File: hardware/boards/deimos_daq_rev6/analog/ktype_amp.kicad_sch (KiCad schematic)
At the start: 12 parts, among them IC9001 INA826AIDR, J9001 AM-K-PCB

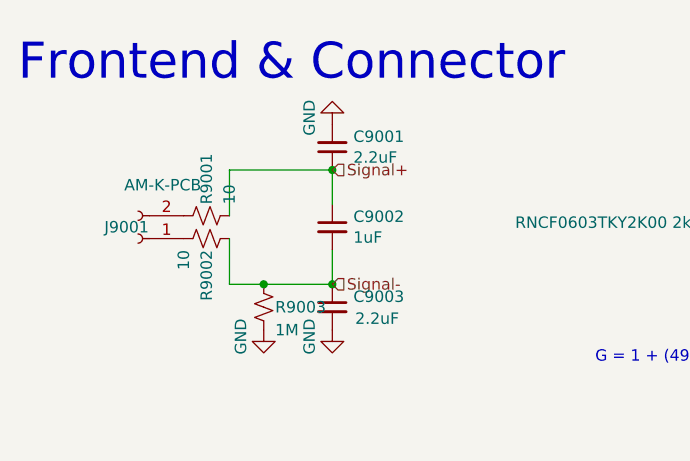
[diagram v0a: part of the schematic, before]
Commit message: move clamp diodes in schematic for filters. Add pulldown on ktype amp.
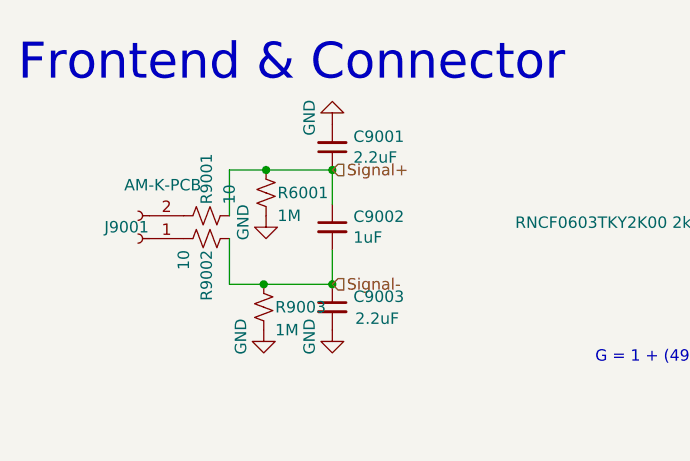
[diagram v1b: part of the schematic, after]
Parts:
- added R6001: 1M, Resistor_SMD:R_0402_1005Metric, symbol Device:R_Small_US
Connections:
- net GND: now also R6001.2
- net Signal+: now also R6001.1
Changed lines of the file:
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@@
+	)
+	(junction
+		(at 117.094 91.44)
+		(diameter 0)
+		(color 0 0 0 0)
 	)
 	(junction
@@
 	(wire
 		(pts
-			(xy 113.03 104.14) (xy 116.84 104.14)
+			(xy 117.094 91.44) (xy 124.46 91.44)
 		)
 		(stroke
@@
 	(wire
 		(pts
-			(xy 219.71 100.33) (xy 252.73 100.33)
+			(xy 113.03 104.14) (xy 116.84 104.14)
 		)
 		(stroke
@@
 	(wire
 		(pts
-			(xy 124.46 95.25) (xy 124.46 91.44)
+			(xy 219.71 100.33) (xy 252.73 100.33)
 		)
 		(stroke
@@
 	(wire
 		(pts
-			(xy 113.03 91.44) (xy 124.46 91.44)
+			(xy 124.46 95.25) (xy 124.46 91.44)
+		)
+		(stroke
+			(width 0)
+			(type default)
+		)
+	)
+	(wire
+		(pts
+			(xy 113.03 91.44) (xy 117.094 91.44)
 		)
 		(stroke
@@
 	)
 	(symbol
+		(lib_id "Device:R_Small_US")
+		(at 117.094 93.98 0)
+		(unit 1)
+		(exclude_from_sim no)
+		(in_bom yes)
+		(on_board yes)
+		(dnp no)
+		(property "Reference" "R6001"
+			(at 118.364 93.98 0)
+			(effects
+				(font
+					(size 1.27 1.27)
+				)
+				(justify left)
+			)
+		)
+		(property "Value" "1M"
+			(at 118.364 96.52 0)
+			(effects
+				(font
+					(size 1.27 1.27)
+				)
+				(justify left)
+			)
+		)
+		(property "Footprint" "Resistor_SMD:R_0402_1005Metric"
+			(at 117.094 93.98 0)
+			(effects
+				(font
+					(size 1.27 1.27)
+				)
+				(hide yes)
+			)
+		)
+		(property "Datasheet" "~"
+			(at 117.094 93.98 0)
+			(effects
+				(font
+					(size 1.27 1.27)
+				)
+				(hide yes)
+			)
+		)
+		(property "Description" ""
+			(at 117.094 93.98 0)
+			(effects
+				(font
+					(size 1.27 1.27)
+				)
+				(hide yes)
+			)
+		)
+		(pin "1"
+		)
+		(pin "2"
+		)
+		(instances
+			(project "analog_frontend_panel"
+				(path "/c241d083-1323-4b4a-a540-956d0afb7b72/15b6c474-02be-417e-bc87-8489b7b45186"
+					(reference "R6001")
+					(unit 1)
+				)
+				(path "/c241d083-1323-4b4a-a540-956d0afb7b72/3688ccee-a1b0-41d3-bce5-95bc73998b83"
+					(reference "R7001")
+					(unit 1)
+				)
+			)
+		)
+	)
+	(symbol
 		(lib_id "Device:C_Small")
 		(at 219.71 107.95 180)
@@
 					(unit 1)
 				)
+			)
+		)
+	)
+	(symbol
+		(lib_id "power:GND")
+		(at 117.094 96.52 0)
+		(unit 1)
+		(exclude_from_sim no)
+		(in_bom yes)
+		(on_board yes)
+		(dnp no)
+		(property "Reference" "#PWR6004"
+			(at 117.094 102.87 0)
+			(effects
+				(font
+					(size 1.27 1.27)
+				)
+				(hide yes)
+			)
+		)
+		(property "Value" "GND"
+			(at 114.554 95.25 90)
+			(effects
+				(font
+					(size 1.27 1.27)
+				)
+				(justify right)
+			)
+		)
+		(property "Footprint" ""
+			(at 117.094 96.52 0)
+			(effects
+				(font
+					(size 1.27 1.27)
+				)
+				(hide yes)
+			)
+		)
+		(property "Datasheet" ""
+			(at 117.094 96.52 0)
+			(effects
+				(font
+					(size 1.27 1.27)
+				)
+				(hide yes)
+			)
+		)
+		(property "Description" ""
+			(at 117.094 96.52 0)
+			(effects
+				(font
+					(size 1.27 1.27)
+				)
+				(hide yes)
+			)
+		)
+		(pin "1"
+		)
+		(instances
+			(project "analog_frontend_panel"
+				(path "/c241d083-1323-4b4a-a540-956d0afb7b72/15b6c474-02be-417e-bc87-8489b7b45186"
+					(reference "#PWR6004")
+					(unit 1)
+				)
+				(path "/c241d083-1323-4b4a-a540-956d0afb7b72/3688ccee-a1b0-41d3-bce5-95bc73998b83"
+					(reference "#PWR7004")
+					(unit 1)
+				)

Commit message: move ovp diodes behind filter amps. wip to implement 5V LDO.
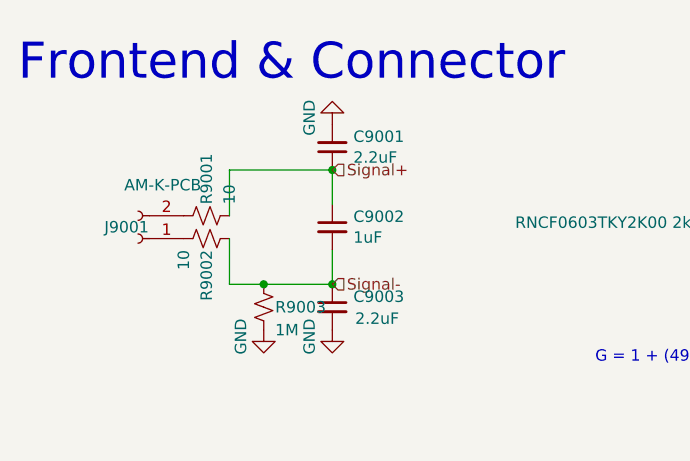
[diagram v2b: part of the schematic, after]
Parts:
- removed R6001: 1M, Resistor_SMD:R_0402_1005Metric, symbol Device:R_Small_US
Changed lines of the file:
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@@
-	)
-	(junction
-		(at 117.094 91.44)
-		(diameter 0)
-		(color 0 0 0 0)
 	)
 	(junction
@@
 	(wire
 		(pts
-			(xy 117.094 91.44) (xy 124.46 91.44)
+			(xy 113.03 91.44) (xy 124.46 91.44)
 		)
 		(stroke
@@
 		(pts
 			(xy 124.46 95.25) (xy 124.46 91.44)
-		)
-		(stroke
-			(width 0)
-			(type default)
-		)
-	)
-	(wire
-		(pts
-			(xy 113.03 91.44) (xy 117.094 91.44)
 		)
 		(stroke
@@
 	)
 	(symbol
-		(lib_id "Device:R_Small_US")
-		(at 117.094 93.98 0)
-		(unit 1)
-		(exclude_from_sim no)
-		(in_bom yes)
-		(on_board yes)
-		(dnp no)
-		(property "Reference" "R6001"
-			(at 118.364 93.98 0)
-			(effects
-				(font
-					(size 1.27 1.27)
-				)
-				(justify left)
-			)
-		)
-		(property "Value" "1M"
-			(at 118.364 96.52 0)
-			(effects
-				(font
-					(size 1.27 1.27)
-				)
-				(justify left)
-			)
-		)
-		(property "Footprint" "Resistor_SMD:R_0402_1005Metric"
-			(at 117.094 93.98 0)
-			(effects
-				(font
-					(size 1.27 1.27)
-				)
-				(hide yes)
-			)
-		)
-		(property "Datasheet" "~"
-			(at 117.094 93.98 0)
-			(effects
-				(font
-					(size 1.27 1.27)
-				)
-				(hide yes)
-			)
-		)
-		(property "Description" ""
-			(at 117.094 93.98 0)
-			(effects
-				(font
-					(size 1.27 1.27)
-				)
-				(hide yes)
-			)
-		)
-		(pin "1"
-		)
-		(pin "2"
-		)
-		(instances
-			(project "analog_frontend_panel"
-				(path "/c241d083-1323-4b4a-a540-956d0afb7b72/15b6c474-02be-417e-bc87-8489b7b45186"
-					(reference "R6001")
-					(unit 1)
-				)
-				(path "/c241d083-1323-4b4a-a540-956d0afb7b72/3688ccee-a1b0-41d3-bce5-95bc73998b83"
-					(reference "R7001")
-					(unit 1)
-				)
-			)
-		)
-	)
-	(symbol
 		(lib_id "Device:C_Small")
 		(at 219.71 107.95 180)
@@
 					(unit 1)
 				)
-			)
-		)
-	)
-	(symbol
-		(lib_id "power:GND")
-		(at 117.094 96.52 0)
-		(unit 1)
-		(exclude_from_sim no)
-		(in_bom yes)
-		(on_board yes)
-		(dnp no)
-		(property "Reference" "#PWR6004"
-			(at 117.094 102.87 0)
-			(effects
-				(font
-					(size 1.27 1.27)
-				)
-				(hide yes)
-			)
-		)
-		(property "Value" "GND"
-			(at 114.554 95.25 90)
-			(effects
-				(font
-					(size 1.27 1.27)
-				)
-				(justify right)
-			)
-		)
-		(property "Footprint" ""
-			(at 117.094 96.52 0)
-			(effects
-				(font
-					(size 1.27 1.27)
-				)
-				(hide yes)
-			)
-		)
-		(property "Datasheet" ""
-			(at 117.094 96.52 0)
-			(effects
-				(font
-					(size 1.27 1.27)
-				)
-				(hide yes)
-			)
-		)
-		(property "Description" ""
-			(at 117.094 96.52 0)
-			(effects
-				(font
-					(size 1.27 1.27)
-				)
-				(hide yes)
-			)
-		)
-		(pin "1"
-		)
-		(instances
-			(project "analog_frontend_panel"
-				(path "/c241d083-1323-4b4a-a540-956d0afb7b72/15b6c474-02be-417e-bc87-8489b7b45186"
-					(reference "#PWR6004")
-					(unit 1)
-				)
-				(path "/c241d083-1323-4b4a-a540-956d0afb7b72/3688ccee-a1b0-41d3-bce5-95bc73998b83"
-					(reference "#PWR7004")
-					(unit 1)
-				)

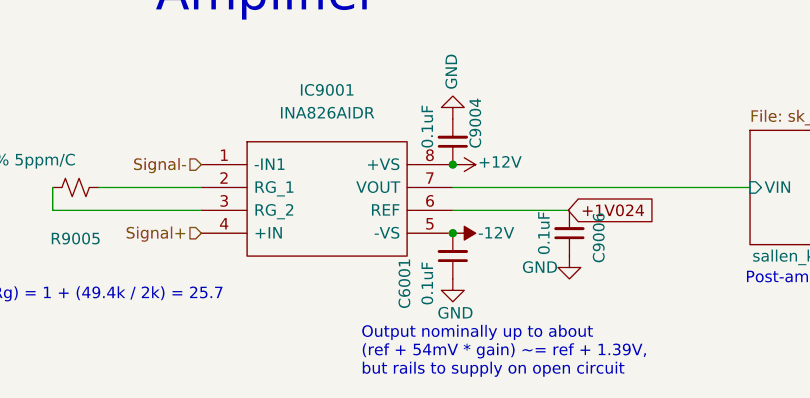
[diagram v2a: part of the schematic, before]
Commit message: exclude testpoints from BOM
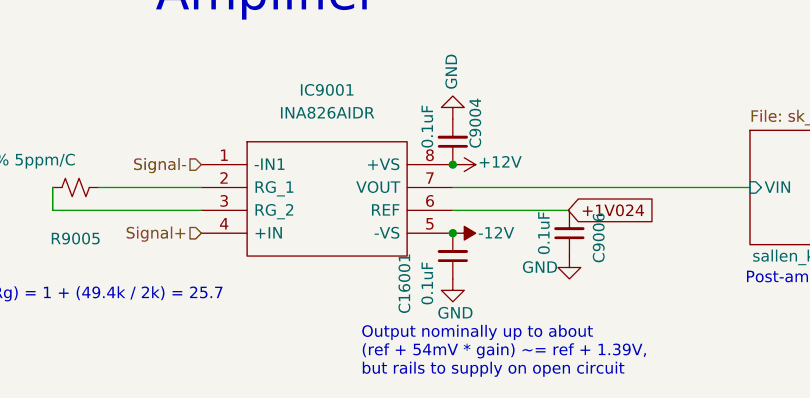
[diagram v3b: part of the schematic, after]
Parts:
- renumbered C6001 to C16001
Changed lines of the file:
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@@
 		(on_board yes)
 		(dnp no)
-		(property "Reference" "#PWR6003"
+		(property "Reference" "#PWR187"
 			(at 219.71 116.84 0)
 			(effects
@@
 		)
 		(instances
+			(project "analog_i"
+				(path "/5a60c4b1-b6cb-416e-8883-8291fa089b87/c2baf18d-2b19-4edb-98b3-535275ee271f/15b6c474-02be-417e-bc87-8489b7b45186"
+					(reference "#PWR187")
+					(unit 1)
+				)
+				(path "/5a60c4b1-b6cb-416e-8883-8291fa089b87/c2baf18d-2b19-4edb-98b3-535275ee271f/3688ccee-a1b0-41d3-bce5-95bc73998b83"
+					(reference "#PWR198")
+					(unit 1)
+				)
+			)
 			(project "analog_frontend_panel"
 				(path "/c241d083-1323-4b4a-a540-956d0afb7b72/15b6c474-02be-417e-bc87-8489b7b45186"
@@
 		(on_board yes)
 		(dnp no)
-		(property "Reference" "#PWR6001"
+		(property "Reference" "#PWR188"
 			(at 215.9 105.41 0)
 			(effects
@@
 		)
 		(instances
+			(project "analog_i"
+				(path "/5a60c4b1-b6cb-416e-8883-8291fa089b87/c2baf18d-2b19-4edb-98b3-535275ee271f/15b6c474-02be-417e-bc87-8489b7b45186"
+					(reference "#PWR188")
+					(unit 1)
+				)
+				(path "/5a60c4b1-b6cb-416e-8883-8291fa089b87/c2baf18d-2b19-4edb-98b3-535275ee271f/3688ccee-a1b0-41d3-bce5-95bc73998b83"
+					(reference "#PWR199")
+					(unit 1)
+				)
+			)
 			(project ""
 				(path "/c241d083-1323-4b4a-a540-956d0afb7b72/15b6c474-02be-417e-bc87-8489b7b45186"
@@
 		(on_board yes)
 		(dnp no)
-		(property "Reference" "#PWR6002"
+		(property "Reference" "#PWR186"
 			(at 215.9 97.79 0)
 			(effects
@@
 		)
 		(instances
+			(project "analog_i"
+				(path "/5a60c4b1-b6cb-416e-8883-8291fa089b87/c2baf18d-2b19-4edb-98b3-535275ee271f/15b6c474-02be-417e-bc87-8489b7b45186"
+					(reference "#PWR186")
+					(unit 1)
+				)
+				(path "/5a60c4b1-b6cb-416e-8883-8291fa089b87/c2baf18d-2b19-4edb-98b3-535275ee271f/3688ccee-a1b0-41d3-bce5-95bc73998b83"
+					(reference "#PWR197")
+					(unit 1)
+				)
+			)
 			(project ""
 				(path "/c241d083-1323-4b4a-a540-956d0afb7b72/15b6c474-02be-417e-bc87-8489b7b45186"
@@
 		(on_board yes)
 		(dnp no)
-		(property "Reference" "C6001"
+		(property "Reference" "C16001"
 			(at 214.376 110.998 90)
 			(effects
@@
 		)
 		(instances
+			(project "analog_i"
+				(path "/5a60c4b1-b6cb-416e-8883-8291fa089b87/c2baf18d-2b19-4edb-98b3-535275ee271f/15b6c474-02be-417e-bc87-8489b7b45186"
+					(reference "C16001")
+					(unit 1)
+				)
+				(path "/5a60c4b1-b6cb-416e-8883-8291fa089b87/c2baf18d-2b19-4edb-98b3-535275ee271f/3688ccee-a1b0-41d3-bce5-95bc73998b83"
+					(reference "C18002")
+					(unit 1)
+				)
+			)
 			(project "analog_frontend_panel"
 				(path "/c241d083-1323-4b4a-a540-956d0afb7b72/15b6c474-02be-417e-bc87-8489b7b45186"
